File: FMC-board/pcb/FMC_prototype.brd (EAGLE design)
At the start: 76.5 x 69 mm, 111 parts, among them Q1 SSM3J328R, U1 4901, U2 7933, U3 ADN4663, U4 ADN4663, U5 ADN4664, U6 PDS1, U7 4901, U8 FMC_SINGLE_WIDTH_MODULE

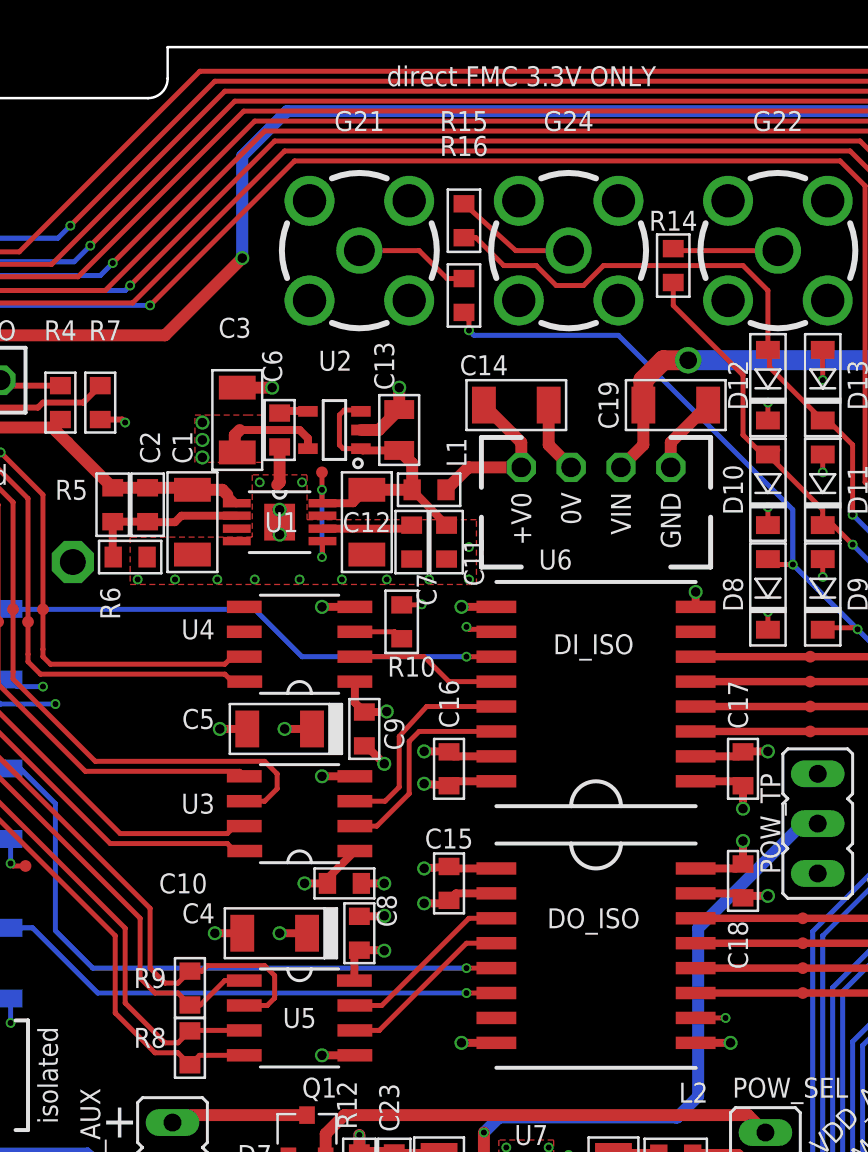
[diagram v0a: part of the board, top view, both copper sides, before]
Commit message: small cleanups on 50ohm line and silkscreen
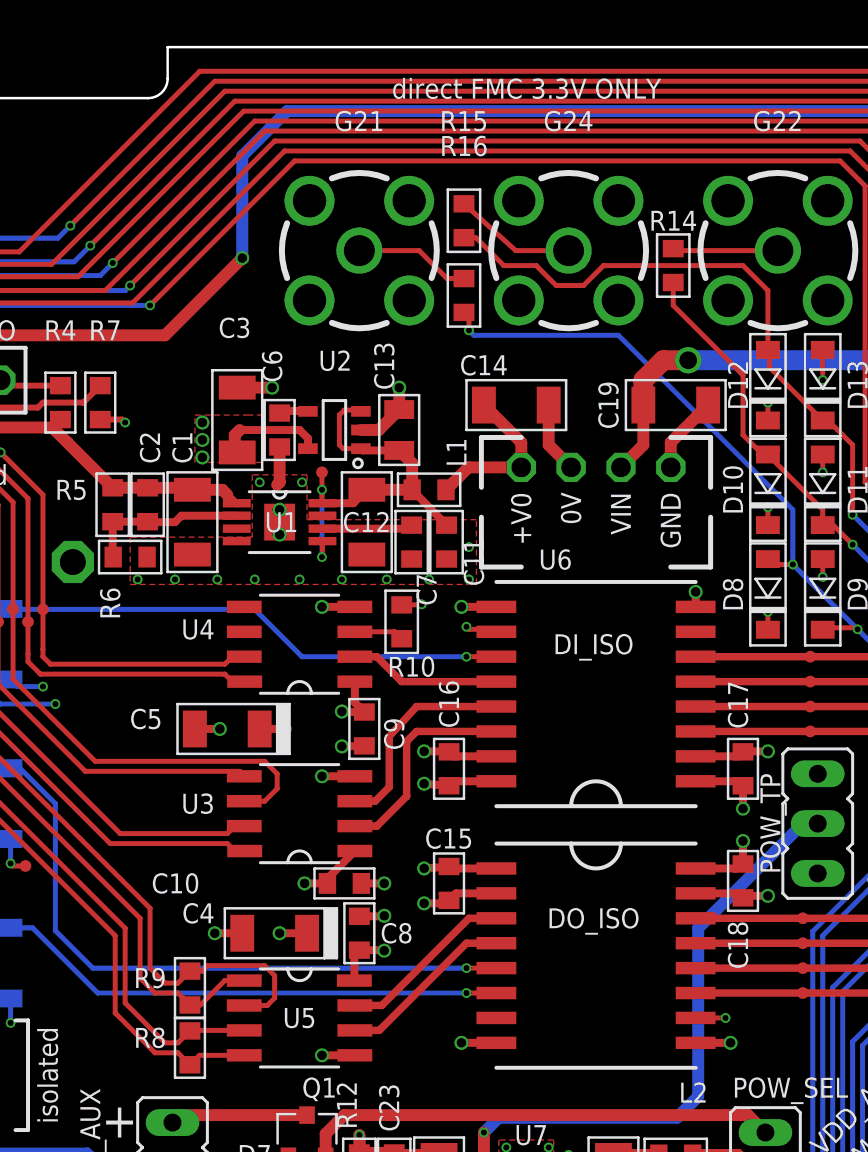
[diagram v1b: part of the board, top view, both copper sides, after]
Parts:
- moved C5 2.67 mm to (-40.3, 31.2)

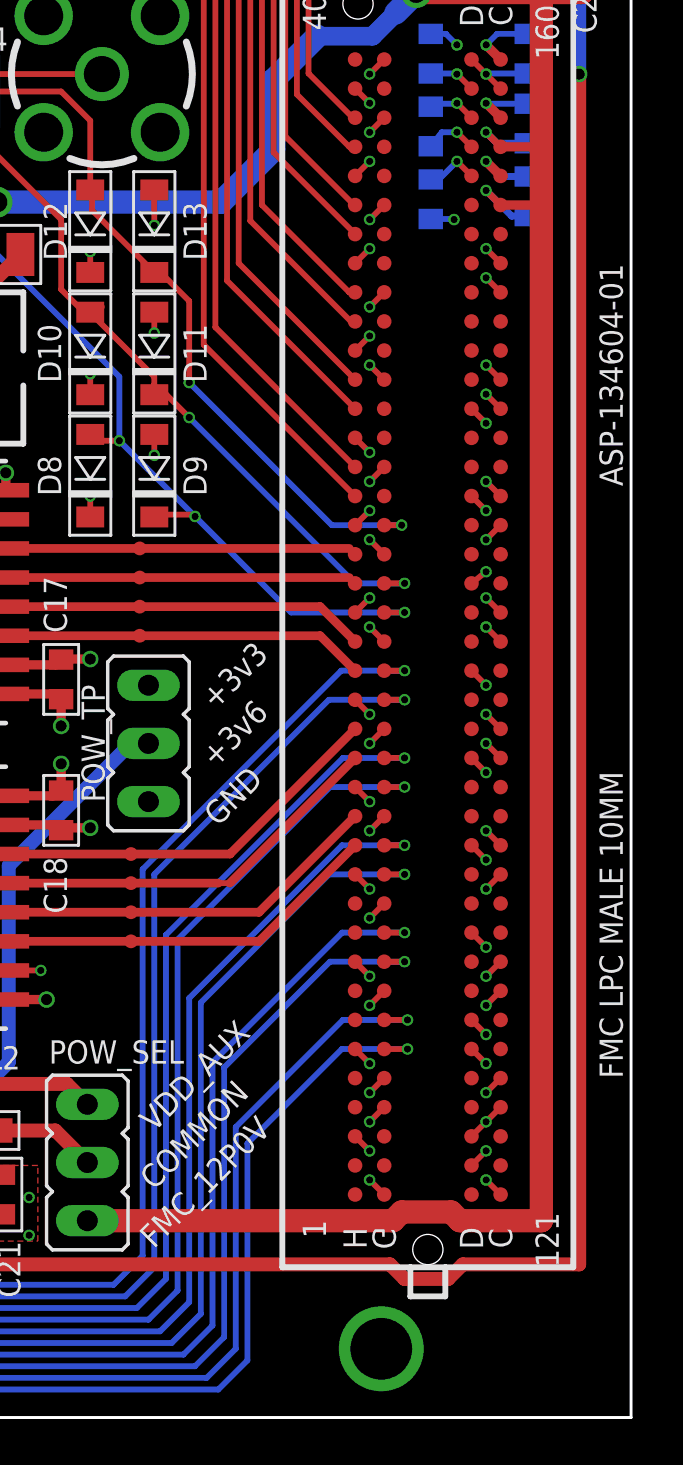
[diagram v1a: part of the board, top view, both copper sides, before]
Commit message: Rerouted MISOB so it does not use _CC lines
- CC means clock capable lines and are intented for a different standard
  than LVDS. They should be fine for LVDS signaling, but we had plenty
  of normal LVDS so better safe than sorry
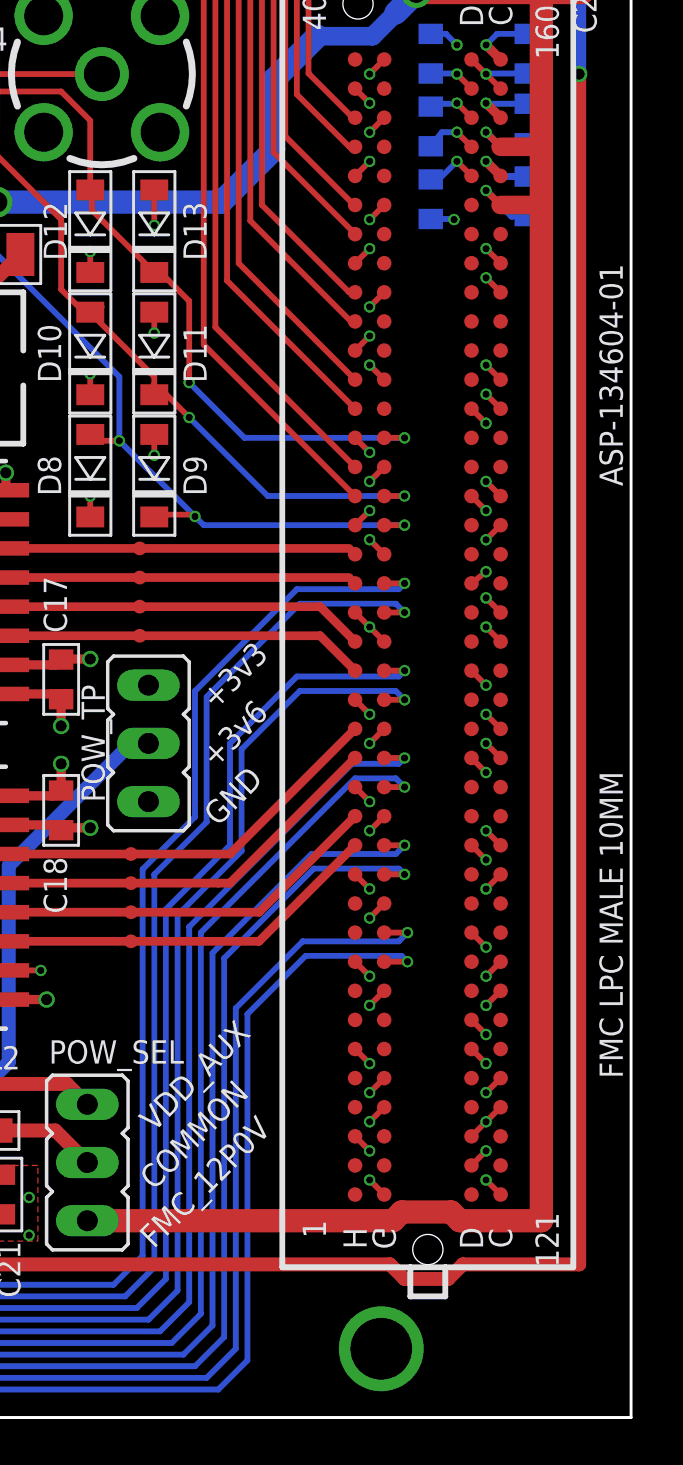
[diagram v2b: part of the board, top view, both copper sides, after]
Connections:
- net A_CS+: now also FMC.P$61; no longer FMC.P$58
- net A_CS-: now also FMC.P$62; no longer FMC.P$59
- net A_MISO1+: now also FMC.P$52; no longer FMC.P$49
- net A_MISO1-: now also FMC.P$53; no longer FMC.P$50
- net A_MISO2+: now also FMC.P$49; no longer FMC.P$46
- net A_MISO2-: now also FMC.P$50; no longer FMC.P$47
- net A_MOSI+: now also FMC.P$55; no longer FMC.P$52
- net A_MOSI-: now also FMC.P$56; no longer FMC.P$53
- net A_SCLK+: now also FMC.P$58; no longer FMC.P$55
- net A_SCLK-: now also FMC.P$59; no longer FMC.P$56
- net G21: now also FMC.P$64; no longer FMC.P$61
- net G22: now also FMC.P$65; no longer FMC.P$62
- net G24: now also FMC.P$67; no longer FMC.P$64
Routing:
- net A_SCLK+: track 86.1 -> 91.2 mm
- net A_MISO2+: track 82.1 -> 87.2 mm
- net A_CS+: track 86.5 -> 91.6 mm
- net A_SCLK-: track 82.2 -> 87.1 mm
- net A_CS-: track 85.0 -> 89.8 mm
- net A_MISO2-: track 76.3 -> 81.0 mm
- net A_MISO1+: track 81.9 -> 86.5 mm
- net A_MISO1-: track 78.1 -> 82.5 mm
- net A_MOSI+: track 86.3 -> 90.0 mm
- net A_MOSI-: track 80.3 -> 83.7 mm
- net G22: track 32.2 -> 30.6 mm
- net G21: track 43.8 -> 42.2 mm
- net G24: track 43.4 -> 42.1 mm
- net GND: vias 85 -> 84

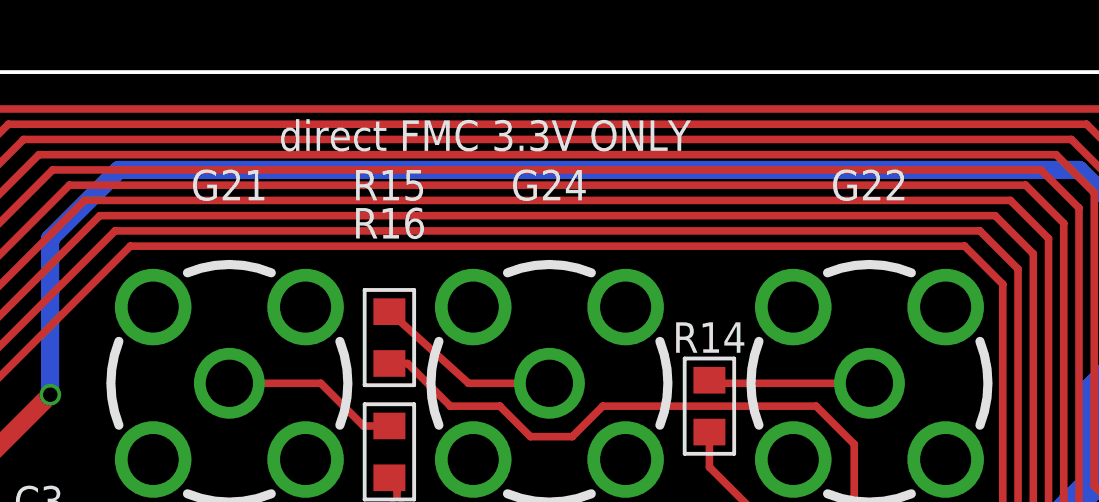
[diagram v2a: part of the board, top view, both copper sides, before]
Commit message: Fixed SMA component names to match new FMC loctaions.
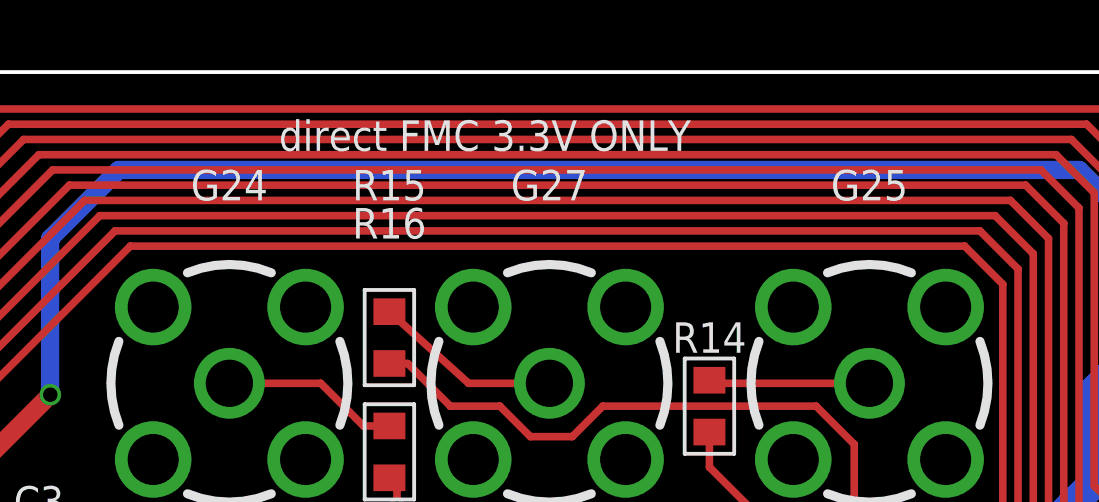
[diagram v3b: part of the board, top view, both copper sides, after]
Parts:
- removed G21: 142-0701, jonnew:SMA_JACK_142-0701-201
- added G27: 142-0701, jonnew:SMA_JACK_142-0701-201
- moved G24 10.7 mm to (-33.5, 55.6)
- renumbered G22 to G25
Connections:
- net G22 renamed G25
- removed net G21: D8.A, D9.C, FMC.P$64, R16.1
- new net G27: D12.A, D13.C, FMC.P$67, R15.1
- net G24: now also D8.A, D9.C, FMC.P$64, R16.1; no longer D12.A, D13.C, FMC.P$67, R15.1
- net GND: now also G27.GND$1, G27.GND$2, G27.GND$3, G27.GND$4; no longer G21.GND$1, G21.GND$2, G21.GND$3, G21.GND$4
- net N$19: now also G27.CLK; no longer G24.CLK
- net N$2: now also G24.CLK; no longer G21.CLK
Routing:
- net G21: track 42.2 -> 0.00 mm, vias 4 -> 0
- net G27: track 0.00 -> 42.1 mm, vias 0 -> 2
- net G24: track 42.1 -> 42.2 mm, vias 2 -> 4
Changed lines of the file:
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@@
 <attribute name="VALUE" x="-13.97" y="30.226" size="1.016" layer="27" font="vector" ratio="18" rot="R270"/>
 </element>
-<element name="G21" library="jonnew" package="SMA_JACK_142-0701-201" value="142-0701" x="-33.528" y="55.626" smashed="yes">
+<element name="G24" library="jonnew" package="SMA_JACK_142-0701-201" value="142-0701" x="-33.528" y="55.626" smashed="yes">
 <attribute name="NAME" x="-33.528" y="62.23" size="1.016" layer="25" font="vector" ratio="18" align="center"/>
 <attribute name="VALUE" x="-33.655" y="60.96" size="1.016" layer="27" font="vector" ratio="18" rot="R180" align="center"/>
 </element>
-<element name="G22" library="jonnew" package="SMA_JACK_142-0701-201" value="142-0701" x="-12.192" y="55.626" smashed="yes">
+<element name="G25" library="jonnew" package="SMA_JACK_142-0701-201" value="142-0701" x="-12.192" y="55.626" smashed="yes">
 <attribute name="NAME" x="-12.192" y="62.23" size="1.016" layer="25" font="vector" ratio="18" align="center"/>
 <attribute name="VALUE" x="-12.065" y="60.96" size="1.016" layer="27" font="vector" ratio="18" align="center"/>
 </element>
-<element name="G24" library="jonnew" package="SMA_JACK_142-0701-201" value="142-0701" x="-22.86" y="55.626" smashed="yes">
+<element name="G27" library="jonnew" package="SMA_JACK_142-0701-201" value="142-0701" x="-22.86" y="55.626" smashed="yes">
 <attribute name="NAME" x="-22.86" y="62.23" size="1.016" layer="25" font="vector" ratio="18" align="center"/>
 <attribute name="VALUE" x="-22.86" y="60.96" size="1.016" layer="27" font="vector" ratio="18" align="center"/>
@@
 <wire x1="3.175" y1="49.3014" x2="2.159" y2="49.3014" width="0.254" layer="16"/>
 <contactref element="POW_TP" pad="3"/>
-<contactref element="G21" pad="GND$4"/>
-<contactref element="G21" pad="GND$1"/>
-<contactref element="G21" pad="GND$3"/>
-<contactref element="G21" pad="GND$2"/>
+<contactref element="G24" pad="GND$4"/>
+<contactref element="G24" pad="GND$1"/>
+<contactref element="G24" pad="GND$3"/>
+<contactref element="G24" pad="GND$2"/>
 <contactref element="D9" pad="A"/>
 <contactref element="D11" pad="A"/>
@@
 <wire x1="-9.906" y1="39.9" x2="-9.73" y2="39.8" width="0.254" layer="1"/>
 <wire x1="-8.89" y1="39.878" x2="-9.398" y2="39.878" width="0.254" layer="2"/>
-<contactref element="G22" pad="GND$3"/>
-<contactref element="G22" pad="GND$4"/>
-<contactref element="G22" pad="GND$1"/>
-<contactref element="G22" pad="GND$2"/>
-<contactref element="G24" pad="GND$3"/>
-<contactref element="G24" pad="GND$4"/>
-<contactref element="G24" pad="GND$1"/>
-<contactref element="G24" pad="GND$2"/>
+<contactref element="G25" pad="GND$3"/>
+<contactref element="G25" pad="GND$4"/>
+<contactref element="G25" pad="GND$1"/>
+<contactref element="G25" pad="GND$2"/>
+<contactref element="G27" pad="GND$3"/>
+<contactref element="G27" pad="GND$4"/>
+<contactref element="G27" pad="GND$1"/>
+<contactref element="G27" pad="GND$2"/>
 <via x="-9.906" y="38.989" extent="1-16" drill="0.3048"/>
 <via x="-9.906" y="44.323" extent="1-16" drill="0.3048"/>
@@
 <wire x1="-51.5366" y1="48.7426" x2="-51.816" y2="49.022" width="0.3048" layer="1"/>
 </signal>
-<signal name="G21">
+<signal name="G24">
 <via x="1.016" y="35.941" extent="1-16" drill="0.3048"/>
 <contactref element="D9" pad="C"/>
@@
 <wire x1="-7.747" y1="35.941" x2="1.016" y2="35.941" width="0.254" layer="16"/>
 </signal>
-<signal name="G22">
+<signal name="G25">
 <via x="1.016" y="37.211" extent="1-16" drill="0.3048"/>
 <contactref element="D11" pad="C"/>
@@
 <wire x1="-4.953" y1="37.211" x2="1.016" y2="37.211" width="0.254" layer="16"/>
 </signal>
-<signal name="G24">
+<signal name="G27">
 <via x="1.016" y="39.751" extent="1-16" drill="0.3048"/>
 <contactref element="D13" pad="C"/>
@@
 </signal>
 <signal name="N$2">
-<contactref element="G21" pad="CLK"/>
+<contactref element="G24" pad="CLK"/>
 <contactref element="R16" pad="2"/>
 <wire x1="-28.194" y1="54.2036" x2="-29.0576" y2="54.2036" width="0.254" layer="1"/>
@@
 </signal>
 <signal name="N$18">
-<contactref element="G22" pad="CLK"/>
+<contactref element="G25" pad="CLK"/>
 <contactref element="R14" pad="2"/>
 <wire x1="-12.192" y1="55.626" x2="-17.4244" y2="55.626" width="0.254" layer="1"/>
@@
 </signal>
 <signal name="N$19">
-<contactref element="G24" pad="CLK"/>
+<contactref element="G27" pad="CLK"/>
 <contactref element="R15" pad="2"/>
 <wire x1="-22.86" y1="55.626" x2="-25.5524" y2="55.626" width="0.254" layer="1"/>

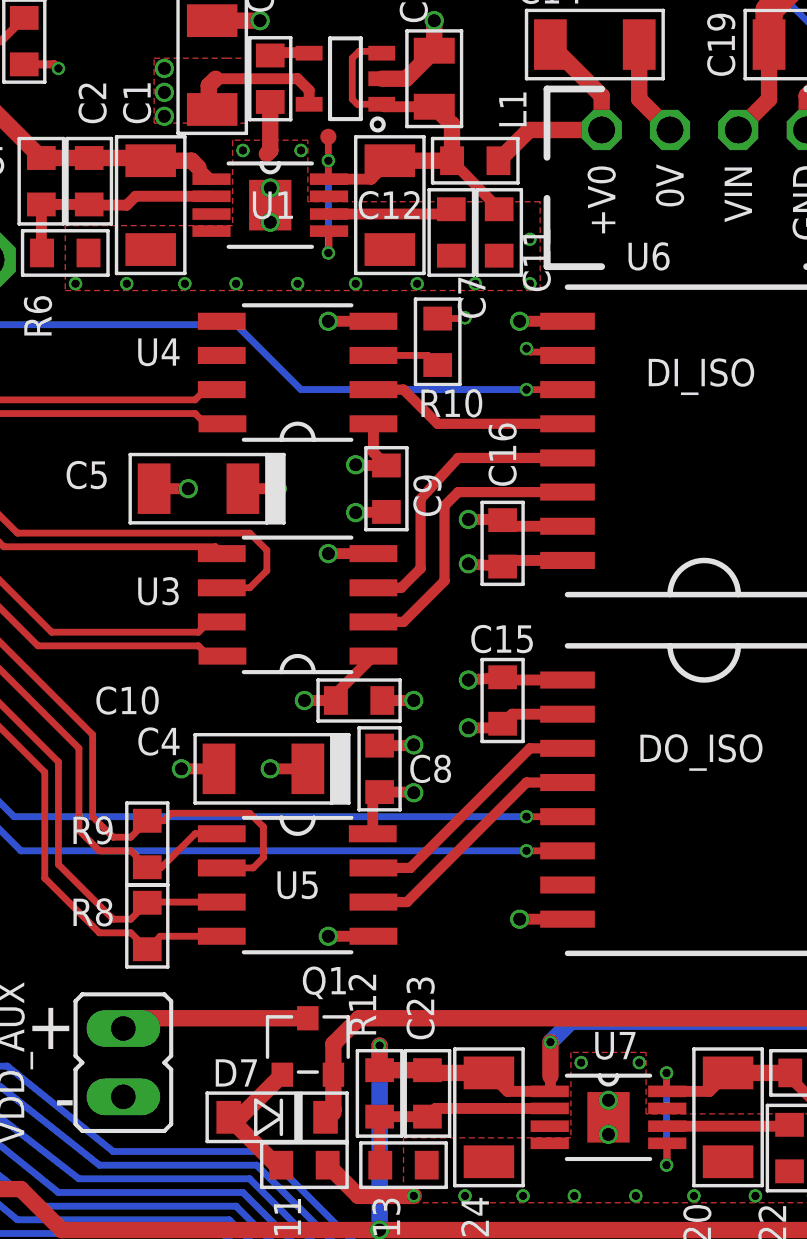
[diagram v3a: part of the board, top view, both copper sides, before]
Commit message: Final changes to layout before fabrication
- Gerbers are being sent to Seeed for fabrication
- I will tag this Rev 0.1
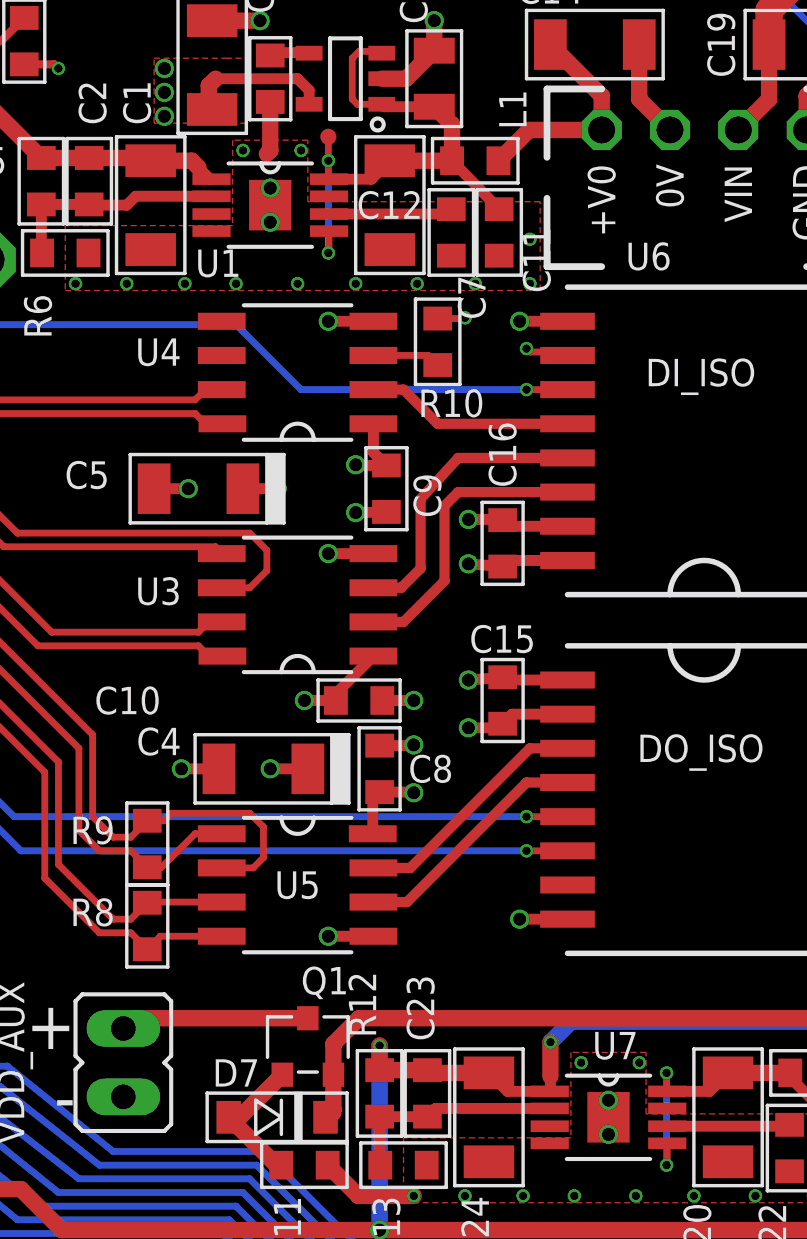
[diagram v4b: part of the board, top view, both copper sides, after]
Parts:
- U1, U7: device puggleboard:SOP65P490X110-9N -> jonnew:SOP65P490X110-9N
